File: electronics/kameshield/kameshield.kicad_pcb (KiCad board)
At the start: 2 copper layers, 31.8 x 67.9 mm, 7 parts, among them P1 CONN_01X15, P2 CONN_01X15, P3 CONN_01X02, P4 CONN_02X03, P5 CONN_02X03, P6 CONN_02X03, P7 CONN_02X03

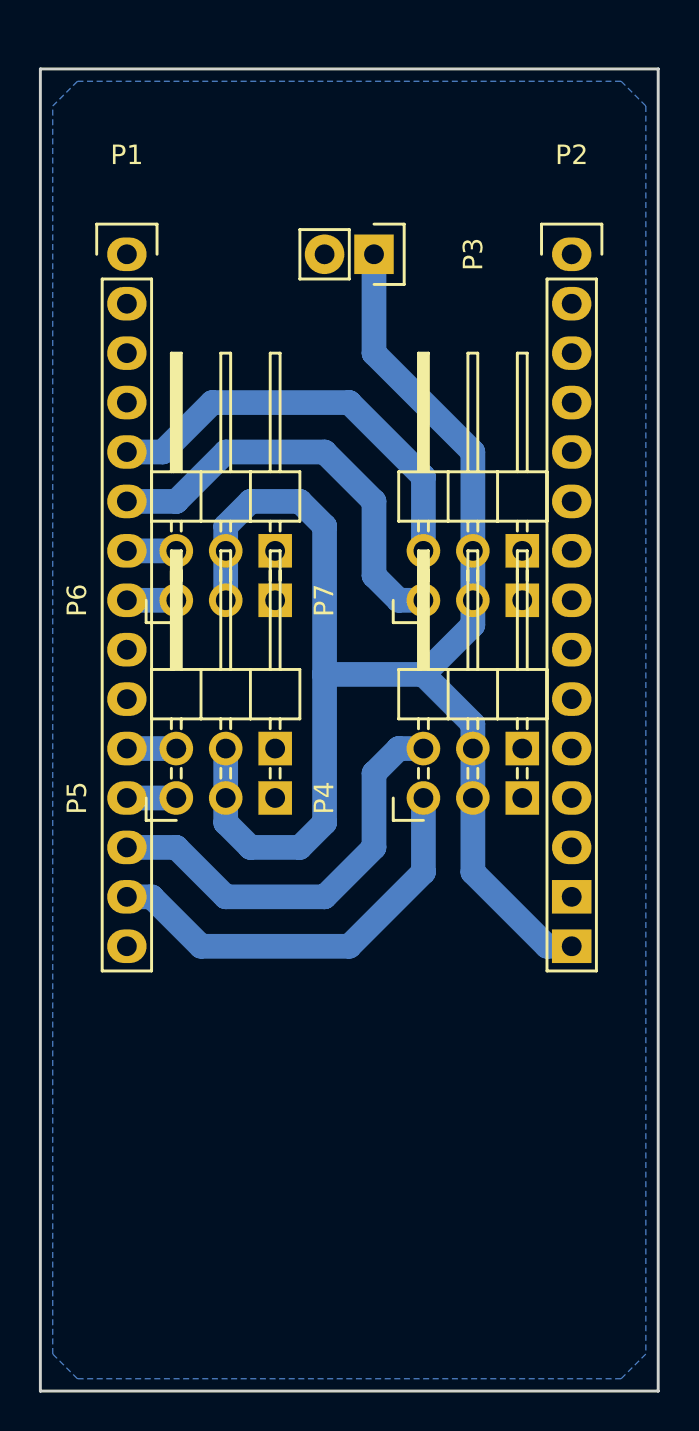
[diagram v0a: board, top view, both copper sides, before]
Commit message: shield for kame
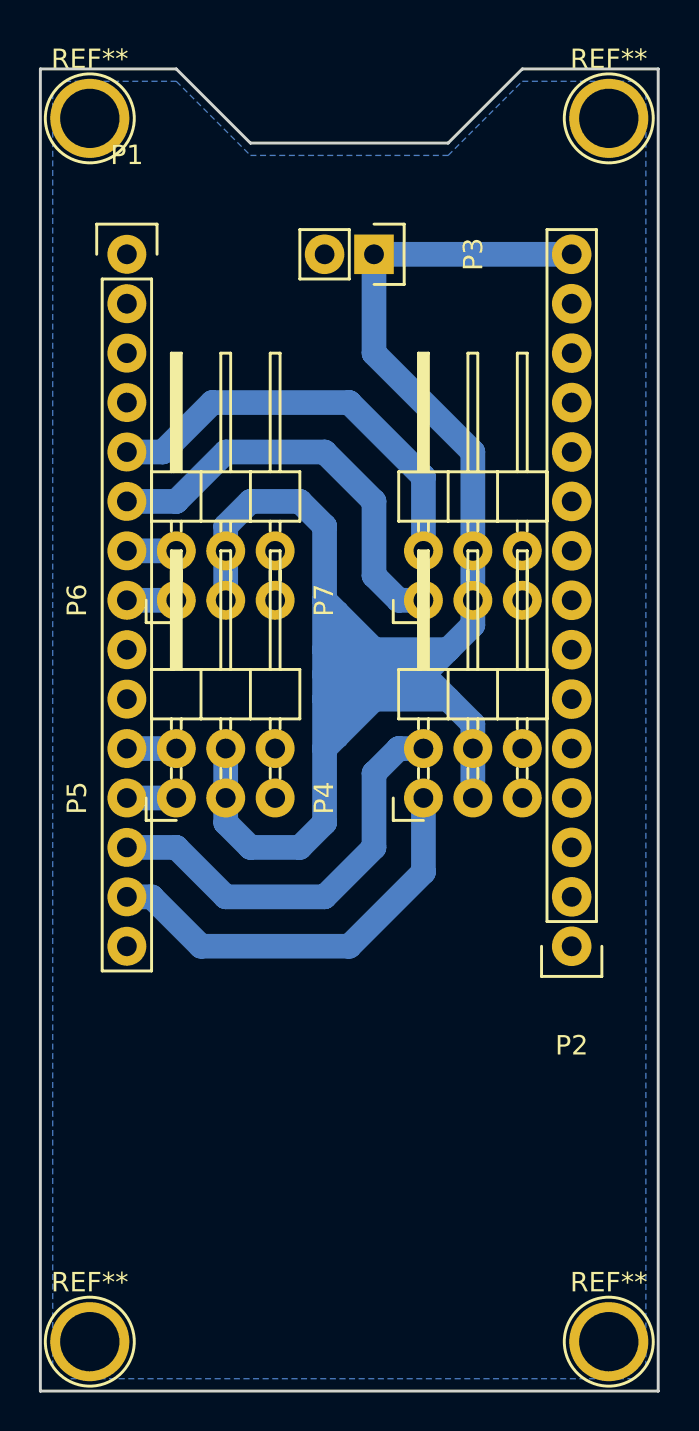
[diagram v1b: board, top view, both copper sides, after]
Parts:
- added REF**: 1pin, Connect:1pin, F.Cu at (109.9, 52.7)
- added REF**: 1pin, Connect:1pin, F.Cu at (83.2, 52.7)
- added REF**: 1pin, Connect:1pin, F.Cu at (83.2, 115.6)
- added REF**: 1pin, Connect:1pin, F.Cu at (109.9, 115.6)
- moved P2 35.6 mm to (108.0, 95.2), turned to 180 degrees
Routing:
- net V+: track 82.8 -> 114.7 mm
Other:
- outline, holes or cut-outs redrawn
